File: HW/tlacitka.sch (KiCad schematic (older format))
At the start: 22 parts, among them SW10 button, SW11 button, SW12 button, SW2 button, SW3 button, SW4 button, SW5 button, SW6 button, SW7 button, SW8 button, SW9 button

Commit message: repair project
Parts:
- renumbered C30 to C11, C36 to C12, C34 to C13, C32 to C14, C17 to C15, C11 to C16, C13 to C17, C15 to C30, C12 to C32, C14 to C34, C16 to C36, SW3 to SW10, SW5 to SW11, SW7 to SW12, SW9 to SW2, SW12 to SW3, SW11 to SW4, SW10 to SW5, SW8 to SW6, SW2 to SW7, SW4 to SW8, SW6 to SW9

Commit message: start place components
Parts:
- renumbered C16 to C11, C17 to C12, C15 to C13, C30 to C14, C14 to C15, C12 to C16, C32 to C17, C34 to C18, C36 to C19, C11 to C20, C13 to C21, SW12 to SW10, SW2 to SW11, SW4 to SW12, SW7 to SW2, SW8 to SW3, SW6 to SW4, SW9 to SW5, SW5 to SW6, SW3 to SW7, SW10 to SW8, SW11 to SW9

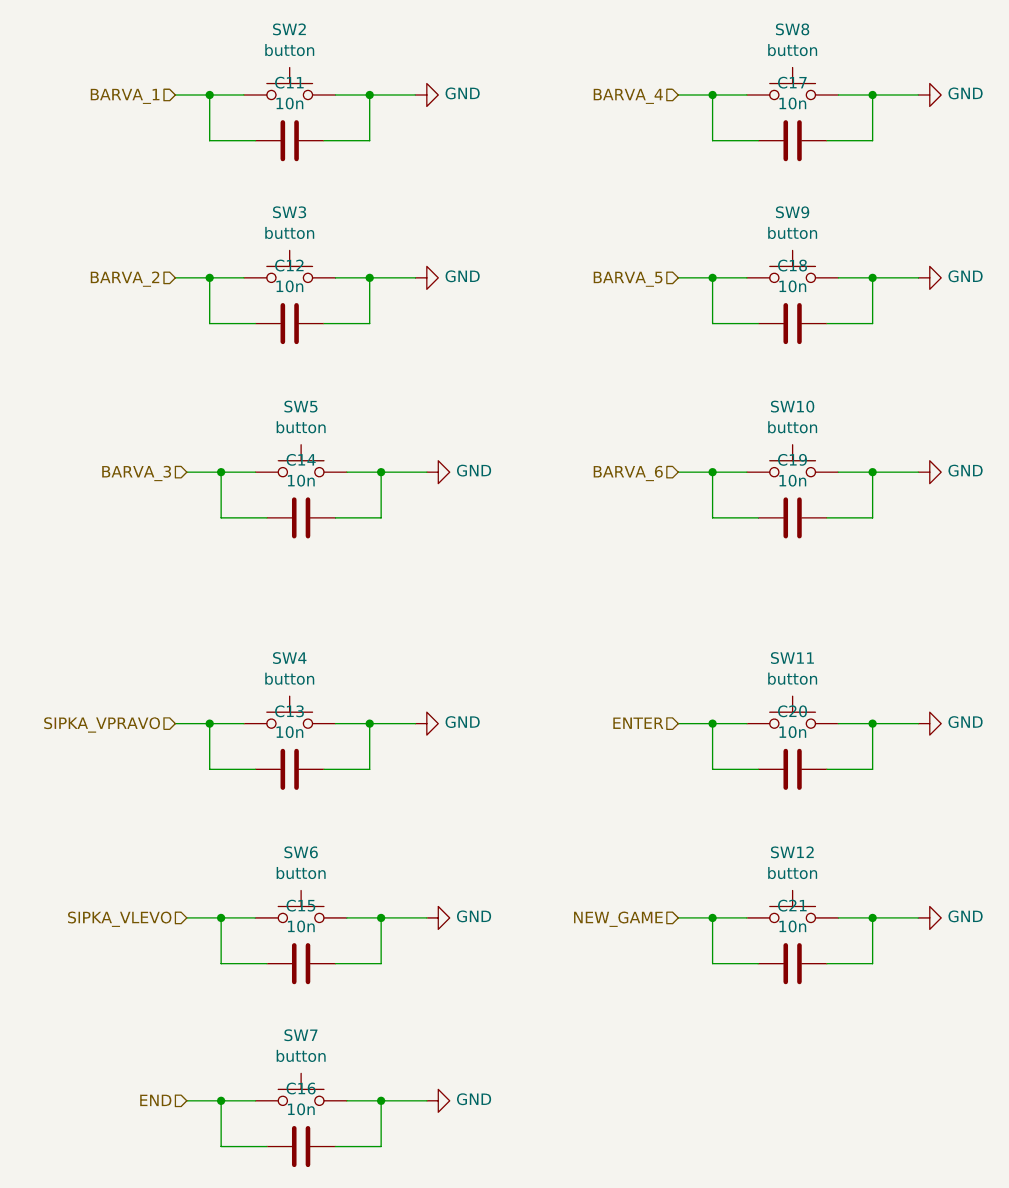
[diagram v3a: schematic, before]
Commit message: change footprint of buttons, continue placing components, repair mistake in power voltage
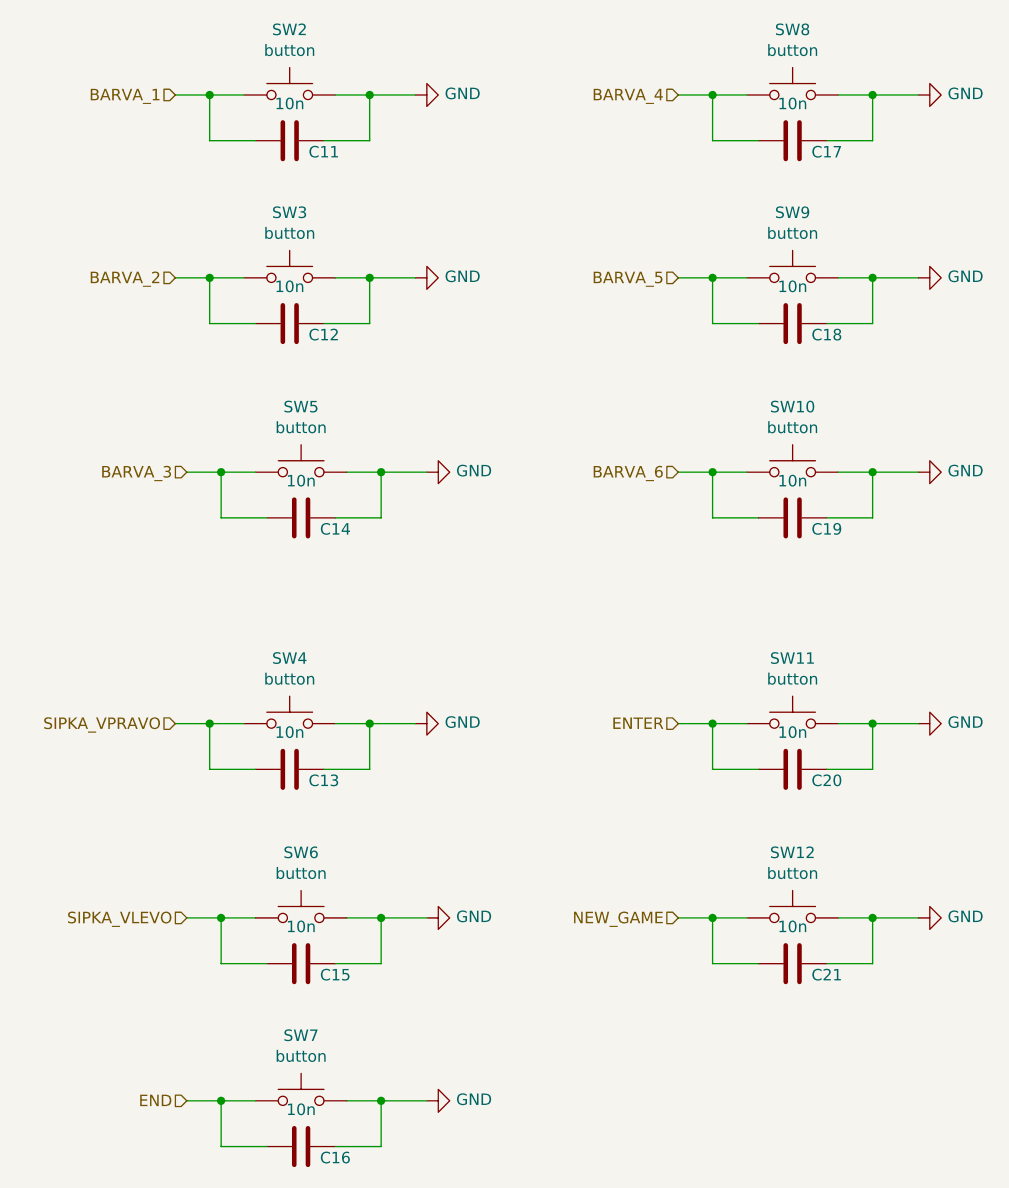
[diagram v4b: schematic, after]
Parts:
- SW10, SW11, SW12, SW2, SW3, SW4, SW5, SW6, SW7, SW8, SW9: footprint Button_Switch_THT:SW_Tactile_Straight_KSL0Axx1LFTR -> Button_Switch_THT:SW_PUSH_6mm
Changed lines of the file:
@@
 F 0 "SW4" H 2200 4235 50  0000 C CNN
 F 1 "button" H 2200 4144 50  0000 C CNN
-F 2 "Button_Switch_THT:SW_Tactile_Straight_KSL0Axx1LFTR" H 2200 4150 50  0001 C CNN
+F 2 "Button_Switch_THT:SW_PUSH_6mm" H 2200 4150 50  0001 C CNN
 F 3 "~" H 2200 4150 50  0001 C CNN
 F 4 "ručně" H 2200 3950 50  0001 C CNN "LCSC"
@@
 AR Path="/5FB92F8B/5F896DFE/5F8DA654" Ref="C?"  Part="1"
 AR Path="/5FB92F8B/5F896E12/5F8DA654" Ref="C?"  Part="1"
-F 0 "C13" V 1948 4150 50  0000 C CNN
+F 0 "C13" V 2250 4300 50  0000 C CNN
 F 1 "10n" V 2039 4150 50  0000 C CNN
 F 2 "Capacitor_SMD:C_0402_1005Metric" H 2238 4000 50  0001 C CNN
@@
 F 0 "SW6" H 2250 5085 50  0000 C CNN
 F 1 "button" H 2250 4994 50  0000 C CNN
-F 2 "Button_Switch_THT:SW_Tactile_Straight_KSL0Axx1LFTR" H 2250 5000 50  0001 C CNN
+F 2 "Button_Switch_THT:SW_PUSH_6mm" H 2250 5000 50  0001 C CNN
 F 3 "~" H 2250 5000 50  0001 C CNN
 F 4 "ručně" H 2250 4800 50  0001 C CNN "LCSC"
@@
 AR Path="/5FB92F8B/5F896DFE/5F8DAC2F" Ref="C?"  Part="1"
 AR Path="/5FB92F8B/5F896E12/5F8DAC2F" Ref="C?"  Part="1"
-F 0 "C15" V 1998 5000 50  0000 C CNN
+F 0 "C15" V 2300 5150 50  0000 C CNN
 F 1 "10n" V 2089 5000 50  0000 C CNN
 F 2 "Capacitor_SMD:C_0402_1005Metric" H 2288 4850 50  0001 C CNN
@@
 F 0 "SW11" H 4400 4235 50  0000 C CNN
 F 1 "button" H 4400 4144 50  0000 C CNN
-F 2 "Button_Switch_THT:SW_Tactile_Straight_KSL0Axx1LFTR" H 4400 4150 50  0001 C CNN
+F 2 "Button_Switch_THT:SW_PUSH_6mm" H 4400 4150 50  0001 C CNN
 F 3 "~" H 4400 4150 50  0001 C CNN
 F 4 "ručně" H 4400 3950 50  0001 C CNN "LCSC"
@@
 AR Path="/5FB92F8B/5F896DFE/5F8DB38E" Ref="C?"  Part="1"
 AR Path="/5FB92F8B/5F896E12/5F8DB38E" Ref="C?"  Part="1"
-F 0 "C20" V 4148 4150 50  0000 C CNN
+F 0 "C20" V 4450 4300 50  0000 C CNN
 F 1 "10n" V 4239 4150 50  0000 C CNN
 F 2 "Capacitor_SMD:C_0402_1005Metric" H 4438 4000 50  0001 C CNN
@@
 F 0 "SW12" H 4400 5085 50  0000 C CNN
 F 1 "button" H 4400 4994 50  0000 C CNN
-F 2 "Button_Switch_THT:SW_Tactile_Straight_KSL0Axx1LFTR" H 4400 5000 50  0001 C CNN
+F 2 "Button_Switch_THT:SW_PUSH_6mm" H 4400 5000 50  0001 C CNN
 F 3 "~" H 4400 5000 50  0001 C CNN
 F 4 "ručně" H 4400 4800 50  0001 C CNN "LCSC"
@@
 AR Path="/5FB92F8B/5F896DFE/5F8DBDA0" Ref="C?"  Part="1"
 AR Path="/5FB92F8B/5F896E12/5F8DBDA0" Ref="C?"  Part="1"
-F 0 "C21" V 4148 5000 50  0000 C CNN
+F 0 "C21" V 4450 5150 50  0000 C CNN
 F 1 "10n" V 4239 5000 50  0000 C CNN
 F 2 "Capacitor_SMD:C_0402_1005Metric" H 4438 4850 50  0001 C CNN
@@
 F 0 "SW3" H 2200 2285 50  0000 C CNN
 F 1 "button" H 2200 2194 50  0000 C CNN
-F 2 "Button_Switch_THT:SW_Tactile_Straight_KSL0Axx1LFTR" H 2200 2200 50  0001 C CNN
+F 2 "Button_Switch_THT:SW_PUSH_6mm" H 2200 2200 50  0001 C CNN
 F 3 "~" H 2200 2200 50  0001 C CNN
 F 4 "ručně" H 2200 2000 50  0001 C CNN "LCSC"
@@
 AR Path="/5FB92F8B/5F896DFE/5F8DF330" Ref="C?"  Part="1"
 AR Path="/5FB92F8B/5F896E12/5F8DF330" Ref="C?"  Part="1"
-F 0 "C12" V 1948 2200 50  0000 C CNN
+F 0 "C12" V 2250 2350 50  0000 C CNN
 F 1 "10n" V 2039 2200 50  0000 C CNN
 F 2 "Capacitor_SMD:C_0402_1005Metric" H 2238 2050 50  0001 C CNN
@@
 F 0 "SW5" H 2250 3135 50  0000 C CNN
 F 1 "button" H 2250 3044 50  0000 C CNN
-F 2 "Button_Switch_THT:SW_Tactile_Straight_KSL0Axx1LFTR" H 2250 3050 50  0001 C CNN
+F 2 "Button_Switch_THT:SW_PUSH_6mm" H 2250 3050 50  0001 C CNN
 F 3 "~" H 2250 3050 50  0001 C CNN
 F 4 "ručně" H 2250 2850 50  0001 C CNN "LCSC"
@@
 AR Path="/5FB92F8B/5F896DFE/5F8DF34E" Ref="C?"  Part="1"
 AR Path="/5FB92F8B/5F896E12/5F8DF34E" Ref="C?"  Part="1"
-F 0 "C14" V 1998 3050 50  0000 C CNN
+F 0 "C14" V 2300 3200 50  0000 C CNN
 F 1 "10n" V 2089 3050 50  0000 C CNN
 F 2 "Capacitor_SMD:C_0402_1005Metric" H 2288 2900 50  0001 C CNN
@@
 F 0 "SW9" H 4400 2285 50  0000 C CNN
 F 1 "button" H 4400 2194 50  0000 C CNN
-F 2 "Button_Switch_THT:SW_Tactile_Straight_KSL0Axx1LFTR" H 4400 2200 50  0001 C CNN
+F 2 "Button_Switch_THT:SW_PUSH_6mm" H 4400 2200 50  0001 C CNN
 F 3 "~" H 4400 2200 50  0001 C CNN
 F 4 "ručně" H 4400 2000 50  0001 C CNN "LCSC"
@@
 AR Path="/5FB92F8B/5F896DFE/5F8DF36C" Ref="C?"  Part="1"
 AR Path="/5FB92F8B/5F896E12/5F8DF36C" Ref="C?"  Part="1"
-F 0 "C18" V 4148 2200 50  0000 C CNN
+F 0 "C18" V 4450 2350 50  0000 C CNN
 F 1 "10n" V 4239 2200 50  0000 C CNN
 F 2 "Capacitor_SMD:C_0402_1005Metric" H 4438 2050 50  0001 C CNN
@@
 F 0 "SW10" H 4400 3135 50  0000 C CNN
 F 1 "button" H 4400 3044 50  0000 C CNN
-F 2 "Button_Switch_THT:SW_Tactile_Straight_KSL0Axx1LFTR" H 4400 3050 50  0001 C CNN
+F 2 "Button_Switch_THT:SW_PUSH_6mm" H 4400 3050 50  0001 C CNN
 F 3 "~" H 4400 3050 50  0001 C CNN
 F 4 "ručně" H 4400 2850 50  0001 C CNN "LCSC"
@@
 AR Path="/5FB92F8B/5F896DFE/5F8DF38A" Ref="C?"  Part="1"
 AR Path="/5FB92F8B/5F896E12/5F8DF38A" Ref="C?"  Part="1"
-F 0 "C19" V 4148 3050 50  0000 C CNN
+F 0 "C19" V 4450 3200 50  0000 C CNN
 F 1 "10n" V 4239 3050 50  0000 C CNN
 F 2 "Capacitor_SMD:C_0402_1005Metric" H 4438 2900 50  0001 C CNN
@@
 F 0 "SW8" H 4400 1485 50  0000 C CNN
 F 1 "button" H 4400 1394 50  0000 C CNN
-F 2 "Button_Switch_THT:SW_Tactile_Straight_KSL0Axx1LFTR" H 4400 1400 50  0001 C CNN
+F 2 "Button_Switch_THT:SW_PUSH_6mm" H 4400 1400 50  0001 C CNN
 F 3 "~" H 4400 1400 50  0001 C CNN
 F 4 "ručně" H 4400 1200 50  0001 C CNN "LCSC"
@@
 AR Path="/5FB92F8B/5F896DFE/5F8E2E9E" Ref="C?"  Part="1"
 AR Path="/5FB92F8B/5F896E12/5F8E2E9E" Ref="C?"  Part="1"
-F 0 "C17" V 4148 1400 50  0000 C CNN
+F 0 "C17" V 4450 1550 50  0000 C CNN
 F 1 "10n" V 4239 1400 50  0000 C CNN
 F 2 "Capacitor_SMD:C_0402_1005Metric" H 4438 1250 50  0001 C CNN
@@
 F 0 "SW7" H 2250 5885 50  0000 C CNN
 F 1 "button" H 2250 5794 50  0000 C CNN
-F 2 "Button_Switch_THT:SW_Tactile_Straight_KSL0Axx1LFTR" H 2250 5800 50  0001 C CNN
+F 2 "Button_Switch_THT:SW_PUSH_6mm" H 2250 5800 50  0001 C CNN
 F 3 "~" H 2250 5800 50  0001 C CNN
 F 4 "ručně" H 2250 5600 50  0001 C CNN "LCSC"
@@
 AR Path="/5FB92F8B/5F896DFE/5F8E616D" Ref="C?"  Part="1"
 AR Path="/5FB92F8B/5F896E12/5F8E616D" Ref="C?"  Part="1"
-F 0 "C16" V 1998 5800 50  0000 C CNN
+F 0 "C16" V 2300 5950 50  0000 C CNN
 F 1 "10n" V 2089 5800 50  0000 C CNN
 F 2 "Capacitor_SMD:C_0402_1005Metric" H 2288 5650 50  0001 C CNN
@@
 F 0 "SW2" H 2200 1485 50  0000 C CNN
 F 1 "button" H 2200 1394 50  0000 C CNN
-F 2 "Button_Switch_THT:SW_Tactile_Straight_KSL0Axx1LFTR" H 2200 1400 50  0001 C CNN
+F 2 "Button_Switch_THT:SW_PUSH_6mm" H 2200 1400 50  0001 C CNN
 F 3 "~" H 2200 1400 50  0001 C CNN
 F 4 "ručně" H 2200 1200 50  0001 C CNN "LCSC"
@@
 AR Path="/5FB92F8B/5F896DFE/5F8E2E80" Ref="C?"  Part="1"
 AR Path="/5FB92F8B/5F896E12/5F8E2E80" Ref="C?"  Part="1"
-F 0 "C11" V 1948 1400 50  0000 C CNN
+F 0 "C11" V 2250 1550 50  0000 C CNN
 F 1 "10n" V 2039 1400 50  0000 C CNN
 F 2 "Capacitor_SMD:C_0402_1005Metric" H 2238 1250 50  0001 C CNN

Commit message: repair footprint of P and N MOS, add order codes for JLCPCB, preparing for fab
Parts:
- C11, C12, C13, C14, C15, C16, C17, C18, C19, C20, C21, SW10, SW11, SW12, SW2, SW3, SW4, SW5, SW6, SW7, SW8, SW9: JLCPCB_CORRECTION (none) -> 0;0;0
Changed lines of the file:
@@
 F 3 "~" H 2200 4150 50  0001 C CNN
 F 4 "ručně" H 2200 3950 50  0001 C CNN "LCSC"
+F 5 "0;0;0" H 2200 3950 50  0001 C CNN "JLCPCB_CORRECTION"
 	1    2200 3950
 	1    0    0    -1
@@
 F 3 "~" H 2200 4150 50  0001 C CNN
 F 4 "C15195" H 2200 4150 50  0001 C CNN "LCSC"
+F 5 "0;0;0" H 2200 4150 50  0001 C CNN "JLCPCB_CORRECTION"
 	1    2200 4150
 	0    1    1    0
@@
 F 3 "~" H 2250 5000 50  0001 C CNN
 F 4 "ručně" H 2250 4800 50  0001 C CNN "LCSC"
+F 5 "0;0;0" H 2250 4800 50  0001 C CNN "JLCPCB_CORRECTION"
 	1    2250 4800
 	1    0    0    -1
@@
 F 3 "~" H 2250 5000 50  0001 C CNN
 F 4 "C15195" H 2250 5000 50  0001 C CNN "LCSC"
+F 5 "0;0;0" H 2250 5000 50  0001 C CNN "JLCPCB_CORRECTION"
 	1    2250 5000
 	0    1    1    0
@@
 F 3 "~" H 4400 4150 50  0001 C CNN
 F 4 "ručně" H 4400 3950 50  0001 C CNN "LCSC"
+F 5 "0;0;0" H 4400 3950 50  0001 C CNN "JLCPCB_CORRECTION"
 	1    4400 3950
 	1    0    0    -1
@@
 F 3 "~" H 4400 4150 50  0001 C CNN
 F 4 "C15195" H 4400 4150 50  0001 C CNN "LCSC"
+F 5 "0;0;0" H 4400 4150 50  0001 C CNN "JLCPCB_CORRECTION"
 	1    4400 4150
 	0    1    1    0
@@
 F 3 "~" H 4400 5000 50  0001 C CNN
 F 4 "ručně" H 4400 4800 50  0001 C CNN "LCSC"
+F 5 "0;0;0" H 4400 4800 50  0001 C CNN "JLCPCB_CORRECTION"
 	1    4400 4800
 	1    0    0    -1
@@
 F 3 "~" H 4400 5000 50  0001 C CNN
 F 4 "C15195" H 4400 5000 50  0001 C CNN "LCSC"
+F 5 "0;0;0" H 4400 5000 50  0001 C CNN "JLCPCB_CORRECTION"
 	1    4400 5000
 	0    1    1    0
@@
 F 3 "~" H 2200 2200 50  0001 C CNN
 F 4 "ručně" H 2200 2000 50  0001 C CNN "LCSC"
+F 5 "0;0;0" H 2200 2000 50  0001 C CNN "JLCPCB_CORRECTION"
 	1    2200 2000
 	1    0    0    -1
@@
 F 3 "~" H 2200 2200 50  0001 C CNN
 F 4 "C15195" H 2200 2200 50  0001 C CNN "LCSC"
+F 5 "0;0;0" H 2200 2200 50  0001 C CNN "JLCPCB_CORRECTION"
 	1    2200 2200
 	0    1    1    0
@@
 F 3 "~" H 2250 3050 50  0001 C CNN
 F 4 "ručně" H 2250 2850 50  0001 C CNN "LCSC"
+F 5 "0;0;0" H 2250 2850 50  0001 C CNN "JLCPCB_CORRECTION"
 	1    2250 2850
 	1    0    0    -1
@@
 F 3 "~" H 2250 3050 50  0001 C CNN
 F 4 "C15195" H 2250 3050 50  0001 C CNN "LCSC"
+F 5 "0;0;0" H 2250 3050 50  0001 C CNN "JLCPCB_CORRECTION"
 	1    2250 3050
 	0    1    1    0
@@
 F 3 "~" H 4400 2200 50  0001 C CNN
 F 4 "ručně" H 4400 2000 50  0001 C CNN "LCSC"
+F 5 "0;0;0" H 4400 2000 50  0001 C CNN "JLCPCB_CORRECTION"
 	1    4400 2000
 	1    0    0    -1
@@
 F 3 "~" H 4400 2200 50  0001 C CNN
 F 4 "C15195" H 4400 2200 50  0001 C CNN "LCSC"
+F 5 "0;0;0" H 4400 2200 50  0001 C CNN "JLCPCB_CORRECTION"
 	1    4400 2200
 	0    1    1    0
@@
 F 3 "~" H 4400 3050 50  0001 C CNN
 F 4 "ručně" H 4400 2850 50  0001 C CNN "LCSC"
+F 5 "0;0;0" H 4400 2850 50  0001 C CNN "JLCPCB_CORRECTION"
 	1    4400 2850
 	1    0    0    -1
@@
 F 3 "~" H 4400 3050 50  0001 C CNN
 F 4 "C15195" H 4400 3050 50  0001 C CNN "LCSC"
+F 5 "0;0;0" H 4400 3050 50  0001 C CNN "JLCPCB_CORRECTION"
 	1    4400 3050
 	0    1    1    0
@@
 F 3 "~" H 4400 1400 50  0001 C CNN
 F 4 "ručně" H 4400 1200 50  0001 C CNN "LCSC"
+F 5 "0;0;0" H 4400 1200 50  0001 C CNN "JLCPCB_CORRECTION"
 	1    4400 1200
 	1    0    0    -1
@@
 F 3 "~" H 4400 1400 50  0001 C CNN
 F 4 "C15195" H 4400 1400 50  0001 C CNN "LCSC"
+F 5 "0;0;0" H 4400 1400 50  0001 C CNN "JLCPCB_CORRECTION"
 	1    4400 1400
 	0    1    1    0
@@
 F 3 "~" H 2250 5800 50  0001 C CNN
 F 4 "ručně" H 2250 5600 50  0001 C CNN "LCSC"
+F 5 "0;0;0" H 2250 5600 50  0001 C CNN "JLCPCB_CORRECTION"
 	1    2250 5600
 	1    0    0    -1
@@
 F 3 "~" H 2250 5800 50  0001 C CNN
 F 4 "C15195" H 2250 5800 50  0001 C CNN "LCSC"
+F 5 "0;0;0" H 2250 5800 50  0001 C CNN "JLCPCB_CORRECTION"
 	1    2250 5800
 	0    1    1    0
@@
 F 3 "~" H 2200 1400 50  0001 C CNN
 F 4 "ručně" H 2200 1200 50  0001 C CNN "LCSC"
+F 5 "0;0;0" H 2200 1200 50  0001 C CNN "JLCPCB_CORRECTION"
 	1    2200 1200
 	1    0    0    -1
@@
 F 3 "~" H 2200 1400 50  0001 C CNN
 F 4 "C15195" H 2200 1400 50  0001 C CNN "LCSC"
+F 5 "0;0;0" H 2200 1400 50  0001 C CNN "JLCPCB_CORRECTION"
 	1    2200 1400
 	0    1    1    0
